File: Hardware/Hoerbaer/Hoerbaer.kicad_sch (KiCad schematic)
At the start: 31 parts, among them J1 I2C, J2 DISPLAY, J3 Micro_SD_Card_Det1, J4 USB1, J5 ENCODER, SW1 RESET, SW2 PROG, U1 ESP32 S3 MINI

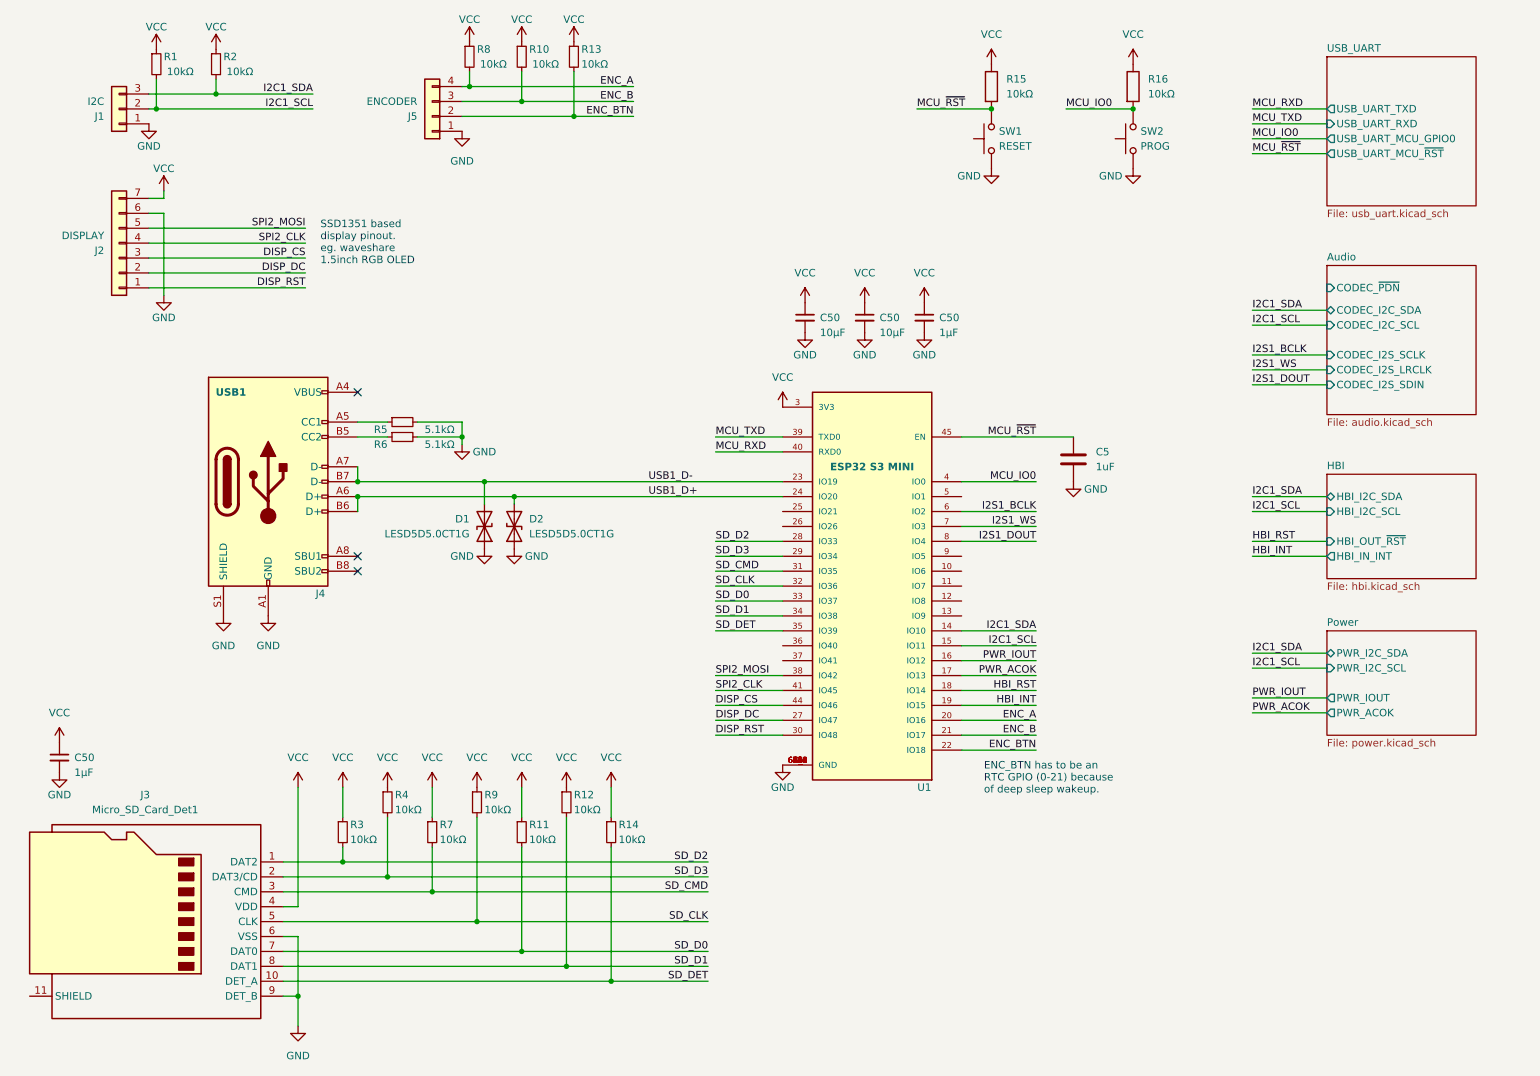
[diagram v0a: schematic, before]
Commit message: Nearly complete schematic with TLV61048 as 12V booster.
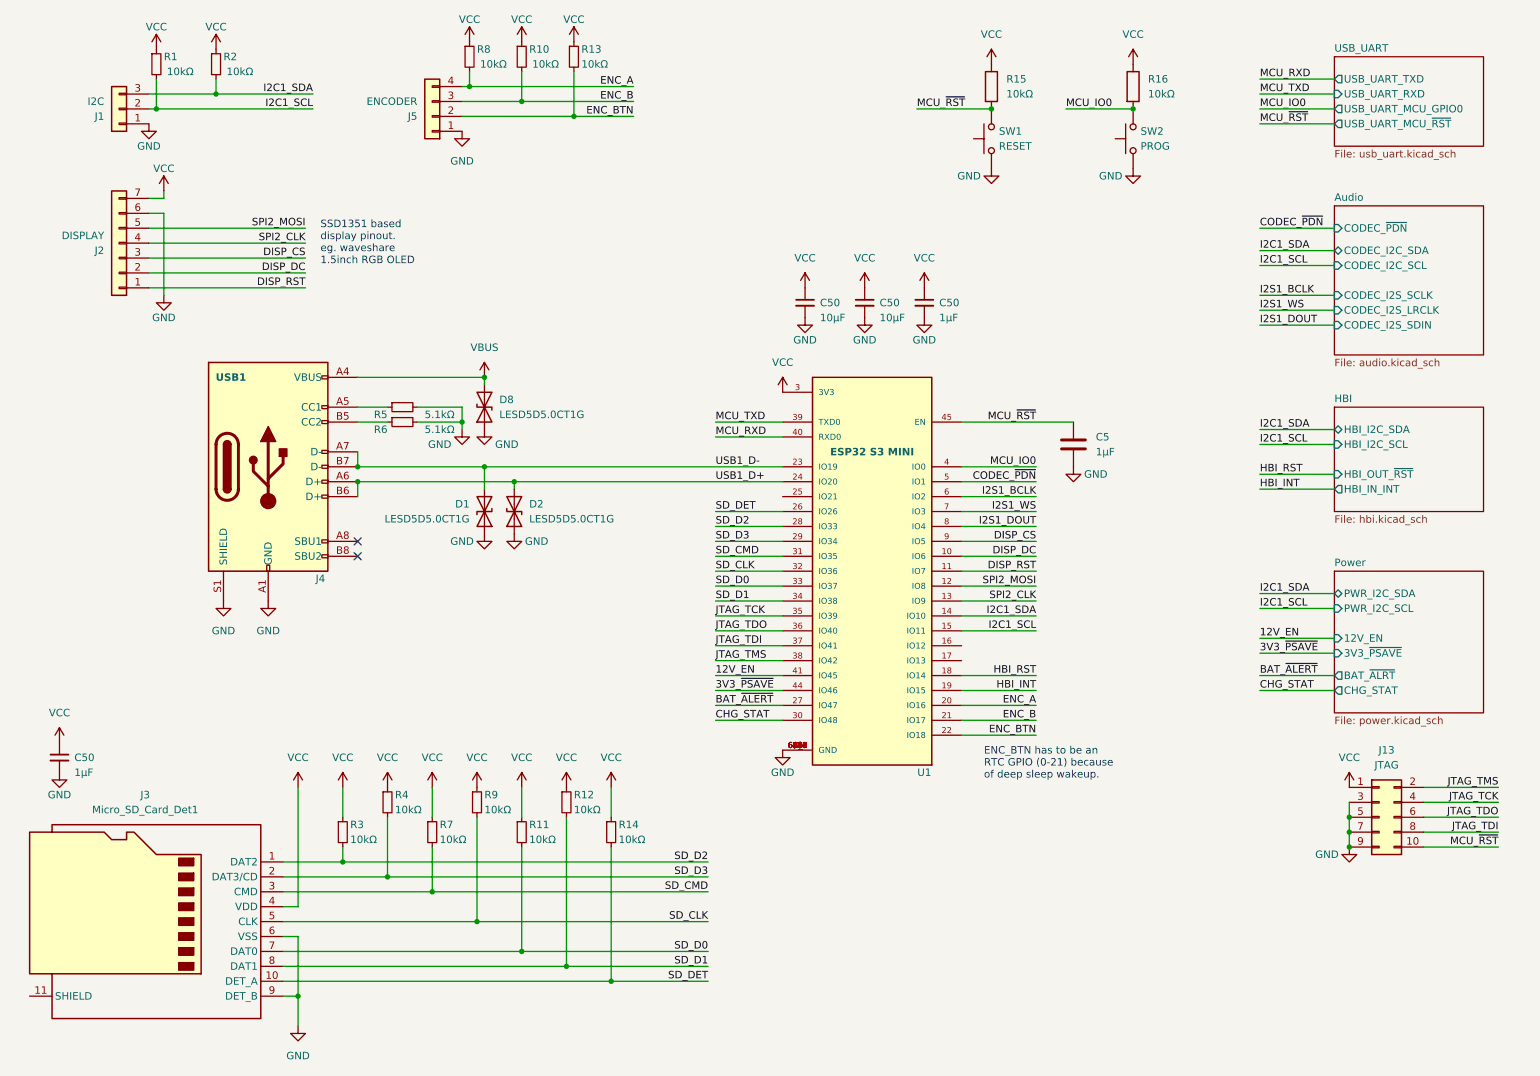
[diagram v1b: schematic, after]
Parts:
- added D8: LESD5D5.0CT1G, Diode_SMD:D_SOD-523, symbol Device:D_TVS
- added J13: JTAG, Connector_PinHeader_1.27mm:PinHeader_2x05_P1.27mm_Vertical_SMD, symbol Connector_Generic:Conn_02x05_Odd_Even
- C5: value 1uF -> 1µF
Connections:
- net DISP_CS: now also U1.9 (IO5); no longer U1.44 (IO46)
- net DISP_DC: now also U1.10 (IO6); no longer U1.27 (IO47)
- net DISP_RST: now also U1.11 (IO7); no longer U1.30 (IO48)
- net GND: now also D8.1 (A1), J13.3 (Pin_3), J13.5 (Pin_5), J13.7 (Pin_7), J13.9 (Pin_9)
- net MCU_~{RST}: now also J13.10 (Pin_10)
- net SD_DET: now also U1.26 (IO26); no longer U1.35 (IO39)
- net SPI2_CLK: now also U1.13 (IO9); no longer U1.41 (IO45)
- net SPI2_MOSI: now also U1.12 (IO8); no longer U1.38 (IO42)
- net VCC: now also J13.1 (Pin_1)
- net JTAG_TDO: now reaches U1.36 (IO40)
- net JTAG_TDO: now also J13.6 (Pin_6)
- net JTAG_TDI: now reaches U1.37 (IO41)
- net JTAG_TDI: now also J13.8 (Pin_8)
- net CODEC_~{PDN}: now reaches U1.5 (IO1)
- net VBUS: now reaches J4.A4 (VBUS), J4.A9 (VBUS), J4.B4 (VBUS), J4.B9 (VBUS)
- net VBUS: now also D8.2 (A2)
- net PWR_ACOK: no longer names the net of U1.17 (IO13)
- net PWR_IOUT: no longer names the net of U1.16 (IO12)
- new net 12V_EN: U1.41 (IO45)
- new net 3V3_~{PSAVE}: U1.44 (IO46)
- new net BAT_~{ALERT}: U1.27 (IO47)
- new net CHG_STAT: U1.30 (IO48)
- new net JTAG_TCK: J13.4 (Pin_4), U1.35 (IO39)
- new net JTAG_TMS: J13.2 (Pin_2), U1.38 (IO42)
- no-connect marks 3 -> 2
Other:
- sheet Power ports: added 12V_EN, 3V3_~{PSAVE}, BAT_~{ALRT}, CHG_STAT; removed PWR_ACOK, PWR_IOUT
- company: (none) -> Drachosaurus Designs
- title: (none) -> Hör Bär main
- moved on the sheet: C5, C50, D1, D2, J4, R5, R6, U1

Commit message: Footprints, order numbers, ...
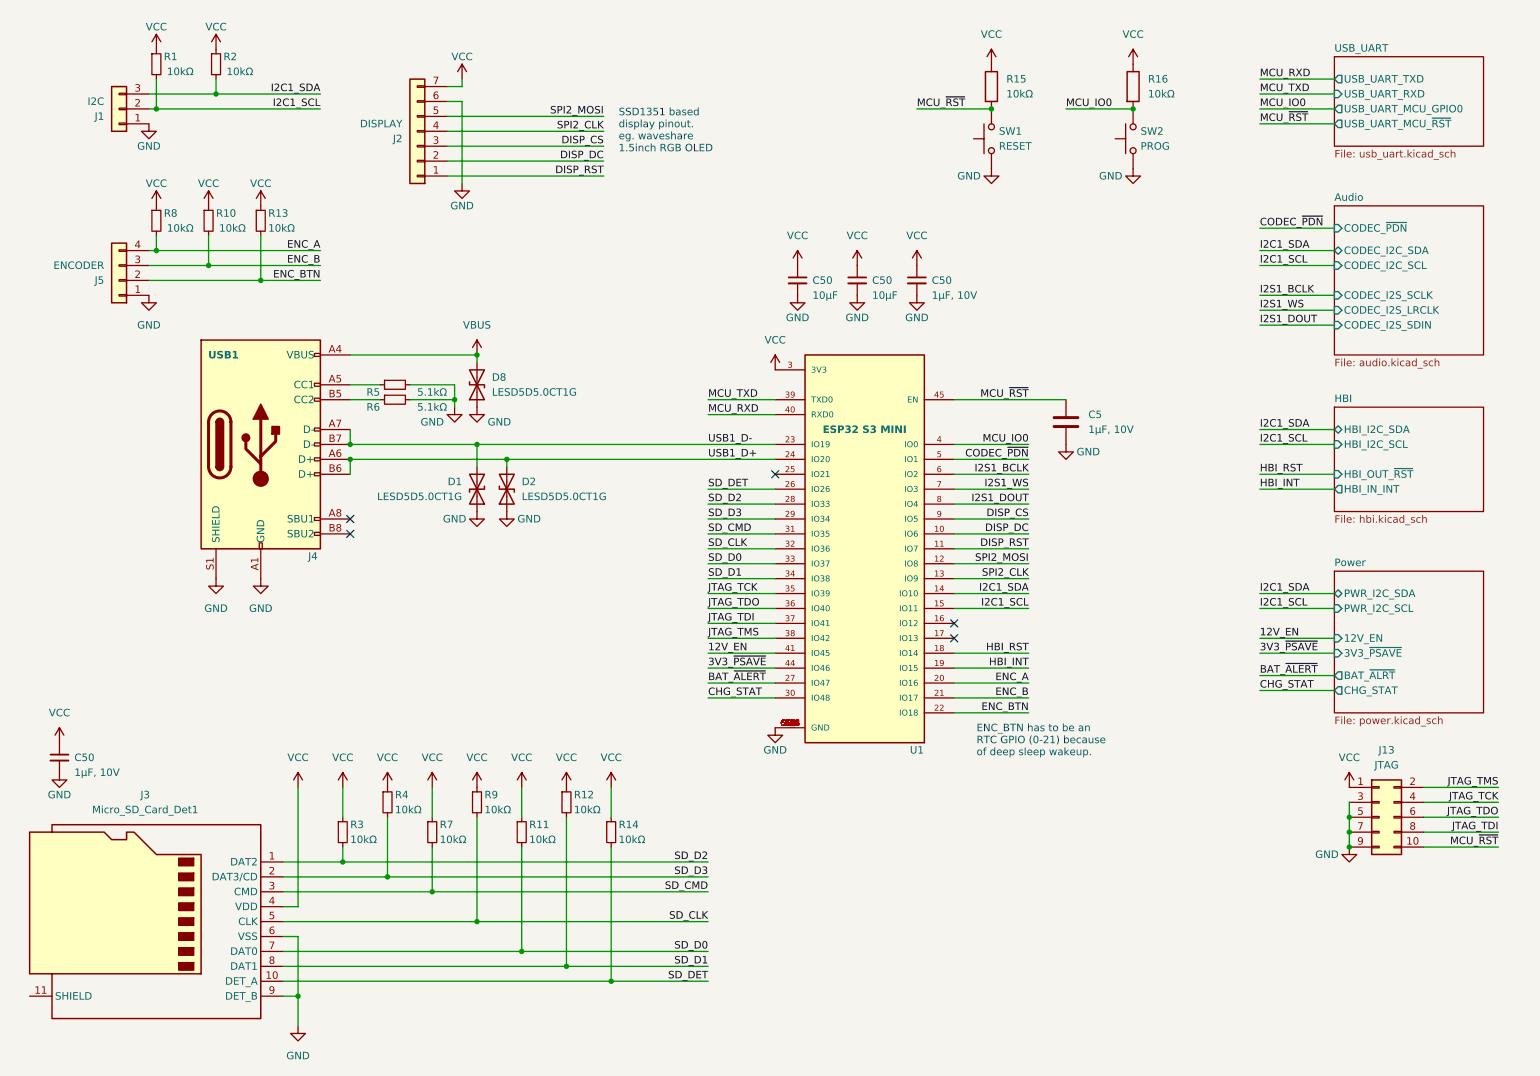
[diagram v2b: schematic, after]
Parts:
- C5, C50: value 1µF -> 1µF, 10V; footprint (none) -> Capacitor_SMD:C_0402_1005Metric; JLCPCB (none) -> C726581; MPN (none) -> AC0805KKX7R6BB105
- C50: footprint (none) -> Capacitor_SMD:C_0805_2012Metric; JLCPCB (none) -> C6119932; MPN (none) -> CGA0805X7R106K250MT
- R1, R10, R11, R12, R13, R14, R15, R16, R2, R3, R4, R5, R6, R7, R8, R9: footprint (none) -> Resistor_SMD:R_0402_1005Metric
- SW1, SW2: footprint (none) -> Baer_Footprints:SW_ TS-1088-AR02016; Availability (none) -> C720477; JLCPCB (none) -> TS-1088-AR02016
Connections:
- no-connect marks 2 -> 5
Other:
- moved on the sheet: C5, C50, D1, D2, D8, J2, J4, J5, R10, R13, R5, R6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

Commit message: More numbers, changed HBI input package, i2c addresses, layout.
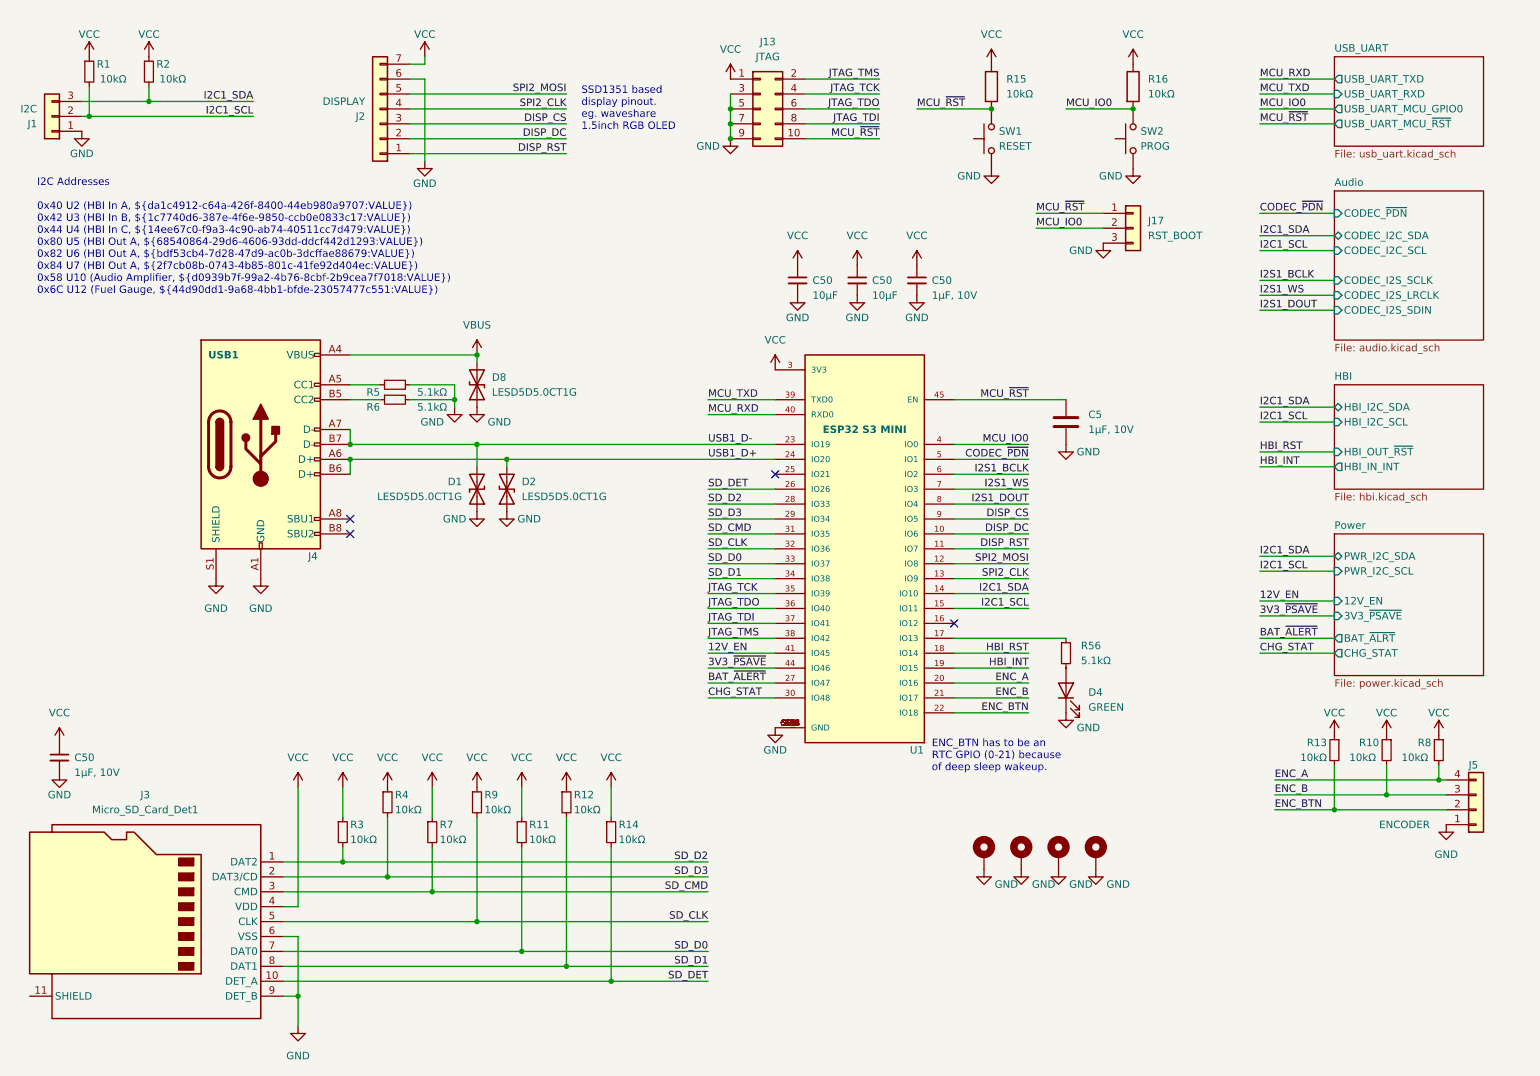
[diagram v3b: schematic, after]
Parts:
- added D4: GREEN, LED_SMD:LED_0603_1608Metric, symbol Device:LED
- added H1, H2, H3, H4: MountingHole_Pad, MountingHole:MountingHole_3.2mm_M3_Pad_Via, symbol Mechanical:MountingHole_Pad
- added J17: RST_BOOT, Connector_PinHeader_2.54mm:PinHeader_1x03_P2.54mm_Vertical, symbol Connector_Generic:Conn_01x03
- added R56: 5.1kΩ, Resistor_SMD:R_0402_1005Metric, symbol Device:R_Small
- J5: footprint Connector_PinHeader_2.54mm:PinHeader_1x03_P2.54mm_Vertical -> Connector_PinHeader_2.54mm:PinHeader_1x04_P2.54mm_Vertical
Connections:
- net GND: now also D4.1 (K), H1.1, H2.1, H3.1, H4.1, J17.3 (Pin_3)
- net MCU_IO0: now also J17.2 (Pin_2)
- net MCU_~{RST}: now also J17.1 (Pin_1)
- net at U1.17 (IO13): now also R56.1
- new net: D4.2 (A), R56.2
- no-connect marks 5 -> 4
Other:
- note added: "I2C Addresses 0x40 U2 (HBI In A, ${da1c4912-c64a-426f-8400-44eb980a9707:VALUE}) 0x42 U3 (HBI In B, ${1c7740d6-387e-4f6e-9850-ccb0e0833c17:VALUE}) 0x44 U4 (HBI In C, ${14ee67c0-f9a3-4c90-ab74-40511cc7d479:VALUE}) 0x80 U5 (HBI Out A, ${68540864-29d6-4606-93dd-ddcf442d1293:VALUE}) 0x82 U6 (HBI Out A, ${bdf53cb4-7d28-47d9-ac0b-3dcffae88679:VALUE}) 0x84 U7 (HBI Out A, ${2f7cb08b-0743-4b85-801c-41fe92d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"
- moved on the sheet: J1, J13, J2, J5, R1, R10, R13, R2, R8

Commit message: Layout drc error free
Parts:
- removed H4: MountingHole_Pad, MountingHole:MountingHole_3.2mm_M3_Pad_Via, symbol Mechanical:MountingHole_Pad
- added C43: 100nF, Capacitor_SMD:C_0402_1005Metric, symbol Device:C_Small
- J1: footprint Connector_PinHeader_2.54mm:PinHeader_1x03_P2.54mm_Vertical -> Connector_PinHeader_2.54mm:PinHeader_1x04_P2.54mm_Vertical; symbol Connector_Generic:Conn_01x03 -> Connector_Generic:Conn_01x04
- U1: footprint Baer_Footprints:XCVR_ESP32-S3-MINI-1-N8 -> ESP32-S3-MINI-1-N8:XCVR_ESP32-S3-MINI-1-N8
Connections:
- net ENC_BTN: now also C43.1
- net GND: now also J3.11 (SHIELD), C43.2
- net VCC: now also J1.4 (Pin_4)
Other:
- note added: "Hardware Debounce (WakeUp pin)"
- moved on the sheet: J2, R1, R2

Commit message: Order numbers
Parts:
- C43: JLCPCB (none) -> C458949; MPN (none) -> MT15B104K160CT
- U1: JLCPCB (none) -> C2913206; MPN (none) -> ESP32-S3-MINI-1-N8
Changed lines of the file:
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@@
       (effects (font (size 1.27 1.27)) (justify bottom) hide)
+    )
+    (property "JLCPCB" "C2913206" (at 168.91 106.68 0)
+      (effects (font (size 1.27 1.27)) hide)
+    )
+    (property "MPN" "ESP32-S3-MINI-1-N8" (at 168.91 106.68 0)
+      (effects (font (size 1.27 1.27)) hide)
     )
     (pin "1")
@@
       (effects (font (size 1.27 1.27)) hide)
     )
+    (property "JLCPCB" "C458949" (at 248.92 153.67 0)
+      (effects (font (size 1.27 1.27)) hide)
+    )
+    (property "MPN" "MT15B104K160CT" (at 248.92 153.67 0)
+      (effects (font (size 1.27 1.27)) hide)
+    )

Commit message: Renamed JLCPCB attribute to LCSC (plugin search list)
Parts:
- C43: JLCPCB C458949 -> (none); LCSC (none) -> C458949
- C5, C50: JLCPCB C726581 -> (none); LCSC (none) -> C726581
- C50: JLCPCB C6119932 -> (none); LCSC (none) -> C6119932
- D1, D2, D8: JLCPCB C383211 -> (none); LCSC (none) -> C383211
- D4: JLCPCB C72043 -> (none); LCSC (none) -> C72043
- J3: JLCPCB C585350 -> (none); LCSC (none) -> C585350
- J4: JLCPCB C2765186 -> (none); LCSC (none) -> C2765186
- SW1, SW2: JLCPCB TS-1088-AR02016 -> (none); LCSC (none) -> TS-1088-AR02016
- U1: JLCPCB C2913206 -> (none); LCSC (none) -> C2913206
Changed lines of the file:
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@@
       (effects (font (size 1.27 1.27)) hide)
     )
-    (property "JLCPCB" "C6119932" (at 157.48 60.96 0)
+    (property "LCSC" "C6119932" (at 157.48 60.96 0)
       (effects (font (size 1.27 1.27)) hide)
     )
@@
       (effects (font (size 1.27 1.27)) hide)
     )
-    (property "JLCPCB" "C383211" (at 107.95 96.52 0)
+    (property "LCSC" "C383211" (at 107.95 96.52 0)
       (effects (font (size 1.27 1.27)) hide)
     )
@@
       (effects (font (size 1.27 1.27)) hide)
     )
-    (property "JLCPCB" "TS-1088-AR02016" (at 190.5 36.83 0)
+    (property "LCSC" "TS-1088-AR02016" (at 190.5 36.83 0)
       (effects (font (size 1.27 1.27)) hide)
     )
@@
       (effects (font (size 1.27 1.27)) hide)
     )
-    (property "JLCPCB" "C72043" (at 203.2 130.81 90)
+    (property "LCSC" "C72043" (at 203.2 130.81 90)
       (effects (font (size 1.27 1.27)) hide)
     )
@@
       (effects (font (size 1.27 1.27)) hide)
     )
-    (property "JLCPCB" "C726581" (at 203.2 85.09 0)
+    (property "LCSC" "C726581" (at 203.2 85.09 0)
       (effects (font (size 1.27 1.27)) hide)
     )
@@
       (effects (font (size 1.27 1.27)) hide)
     )
-    (property "JLCPCB" "C585350" (at 46.99 170.18 0)
+    (property "LCSC" "C585350" (at 46.99 170.18 0)
       (effects (font (size 1.27 1.27)) hide)
     )
@@
       (effects (font (size 1.27 1.27)) hide)
     )
-    (property "JLCPCB" "C383211" (at 102.87 78.74 0)
+    (property "LCSC" "C383211" (at 102.87 78.74 0)
       (effects (font (size 1.27 1.27)) hide)
     )
@@
       (effects (font (size 1.27 1.27)) (justify bottom) hide)
     )
-    (property "JLCPCB" "C2913206" (at 168.91 106.68 0)
+    (property "LCSC" "C2913206" (at 168.91 106.68 0)
       (effects (font (size 1.27 1.27)) hide)
     )
@@
       (effects (font (size 1.27 1.27)) hide)
     )
-    (property "JLCPCB" "C2765186" (at 66.04 88.9 0)
+    (property "LCSC" "C2765186" (at 66.04 88.9 0)
       (effects (font (size 1.27 1.27)) hide)
     )
@@
       (effects (font (size 1.27 1.27)) hide)
     )
-    (property "JLCPCB" "C726581" (at 31.75 142.24 0)
+    (property "LCSC" "C726581" (at 31.75 142.24 0)
       (effects (font (size 1.27 1.27)) hide)
     )
@@
       (effects (font (size 1.27 1.27)) hide)
     )
-    (property "JLCPCB" "C383211" (at 102.87 96.52 0)
+    (property "LCSC" "C383211" (at 102.87 96.52 0)
       (effects (font (size 1.27 1.27)) hide)
     )
@@
       (effects (font (size 1.27 1.27)) hide)
     )
-    (property "JLCPCB" "TS-1088-AR02016" (at 214.63 36.83 0)
+    (property "LCSC" "TS-1088-AR02016" (at 214.63 36.83 0)
       (effects (font (size 1.27 1.27)) hide)
     )
@@
       (effects (font (size 1.27 1.27)) hide)
     )
-    (property "JLCPCB" "C6119932" (at 167.64 60.96 0)
+    (property "LCSC" "C6119932" (at 167.64 60.96 0)
       (effects (font (size 1.27 1.27)) hide)
     )
@@
       (effects (font (size 1.27 1.27)) hide)
     )
-    (property "JLCPCB" "C726581" (at 177.8 60.96 0)
+    (property "LCSC" "C726581" (at 177.8 60.96 0)
       (effects (font (size 1.27 1.27)) hide)
     )
@@
       (effects (font (size 1.27 1.27)) hide)
     )
-    (property "JLCPCB" "C458949" (at 248.92 153.67 0)
-      (effects (font (size 1.27 1.27)) hide)
-    )
+    (property "LCSC" "C458949" (at 248.92 153.67 0)
+      (effects (font (size 1.27 1.27)) hide)
+    )
